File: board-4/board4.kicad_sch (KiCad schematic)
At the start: 101 parts, among them CN1 B2B-PH-K-S(LF)(SN), Q1 DMG3415U, SW1 B3U-1000P, SW2 B3U-1000P, U1 SY8088IAAC, U10 AT42QT1011-TSHR, U12 MX35LF1GE4AB-Z4ITR, U3 MCP73831T-2ACI/OT, U4 TPS61022RWUR, U5 ESP32-S3-MINI-1-N4R2, U6 SN74LV1T34DBVR, U7 MAX98357AETE+T, U8 SPH0655LM4H-1-8, U9 MAX17048G+T10

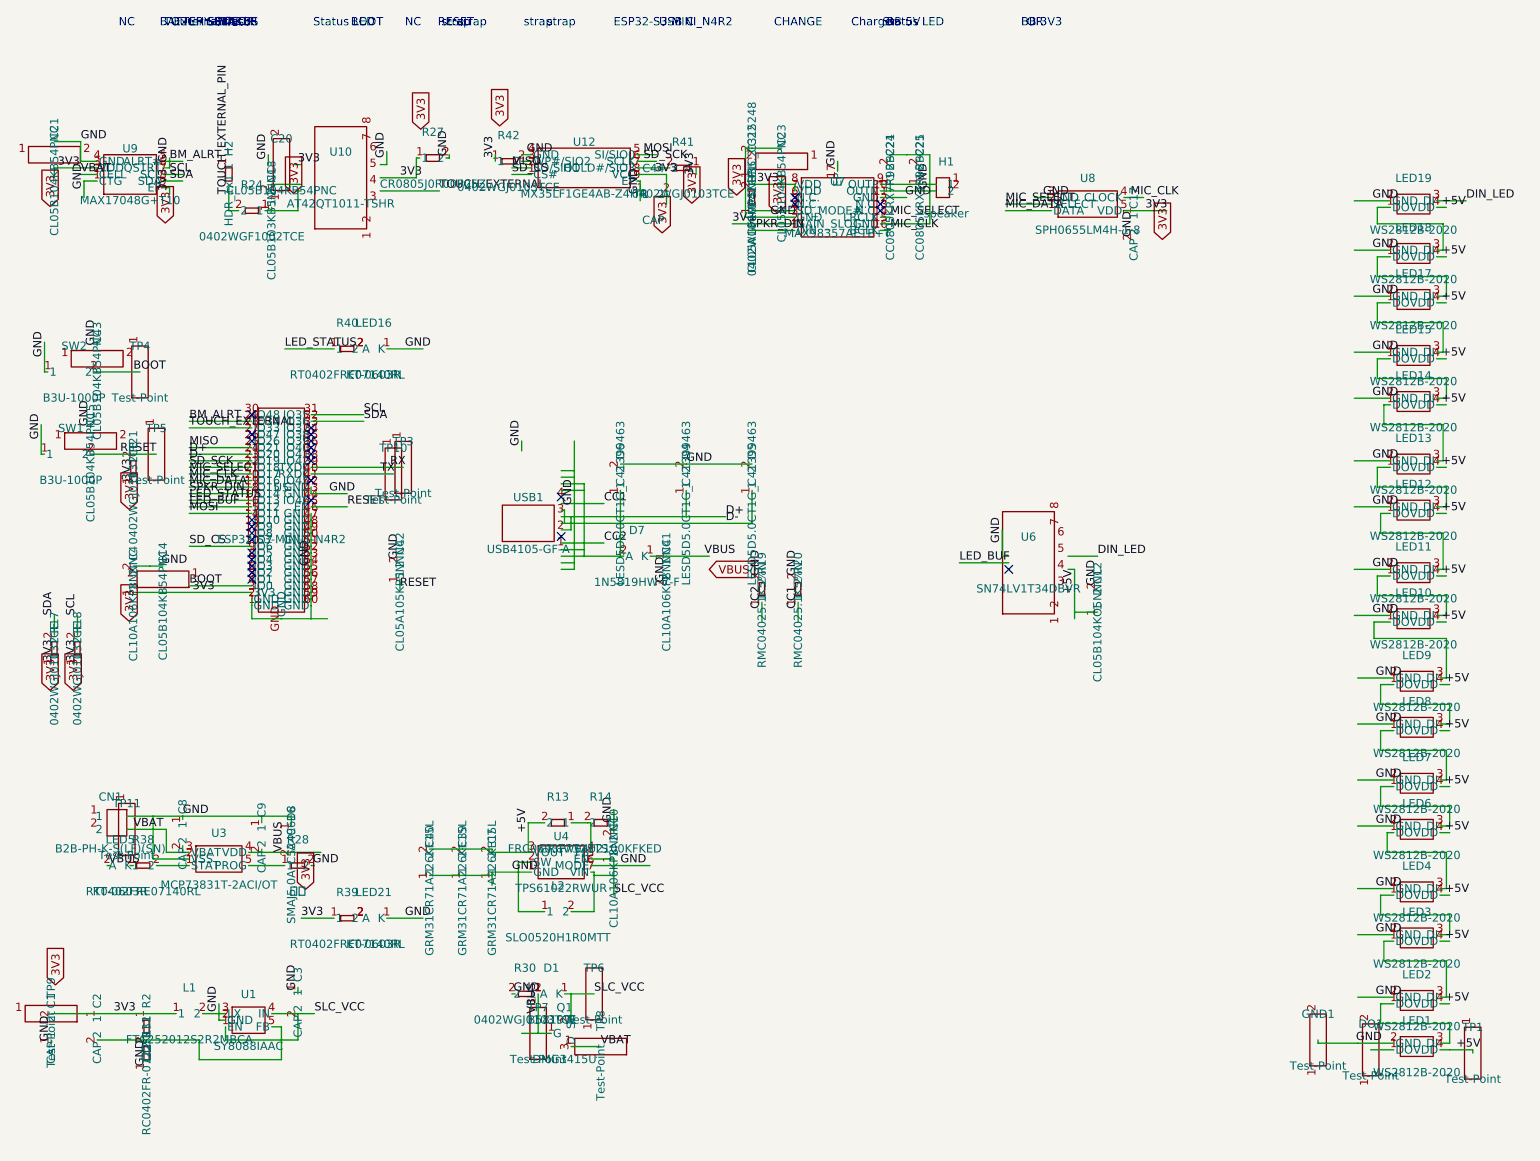
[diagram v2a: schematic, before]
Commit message: Schematic: device-table fallback for symbol UUIDs — 44/44 components now use real .esym geometry (was 39/44, the 5 missing had no explicit Symbol attr). Wire endpoints should now land on real pin offsets.
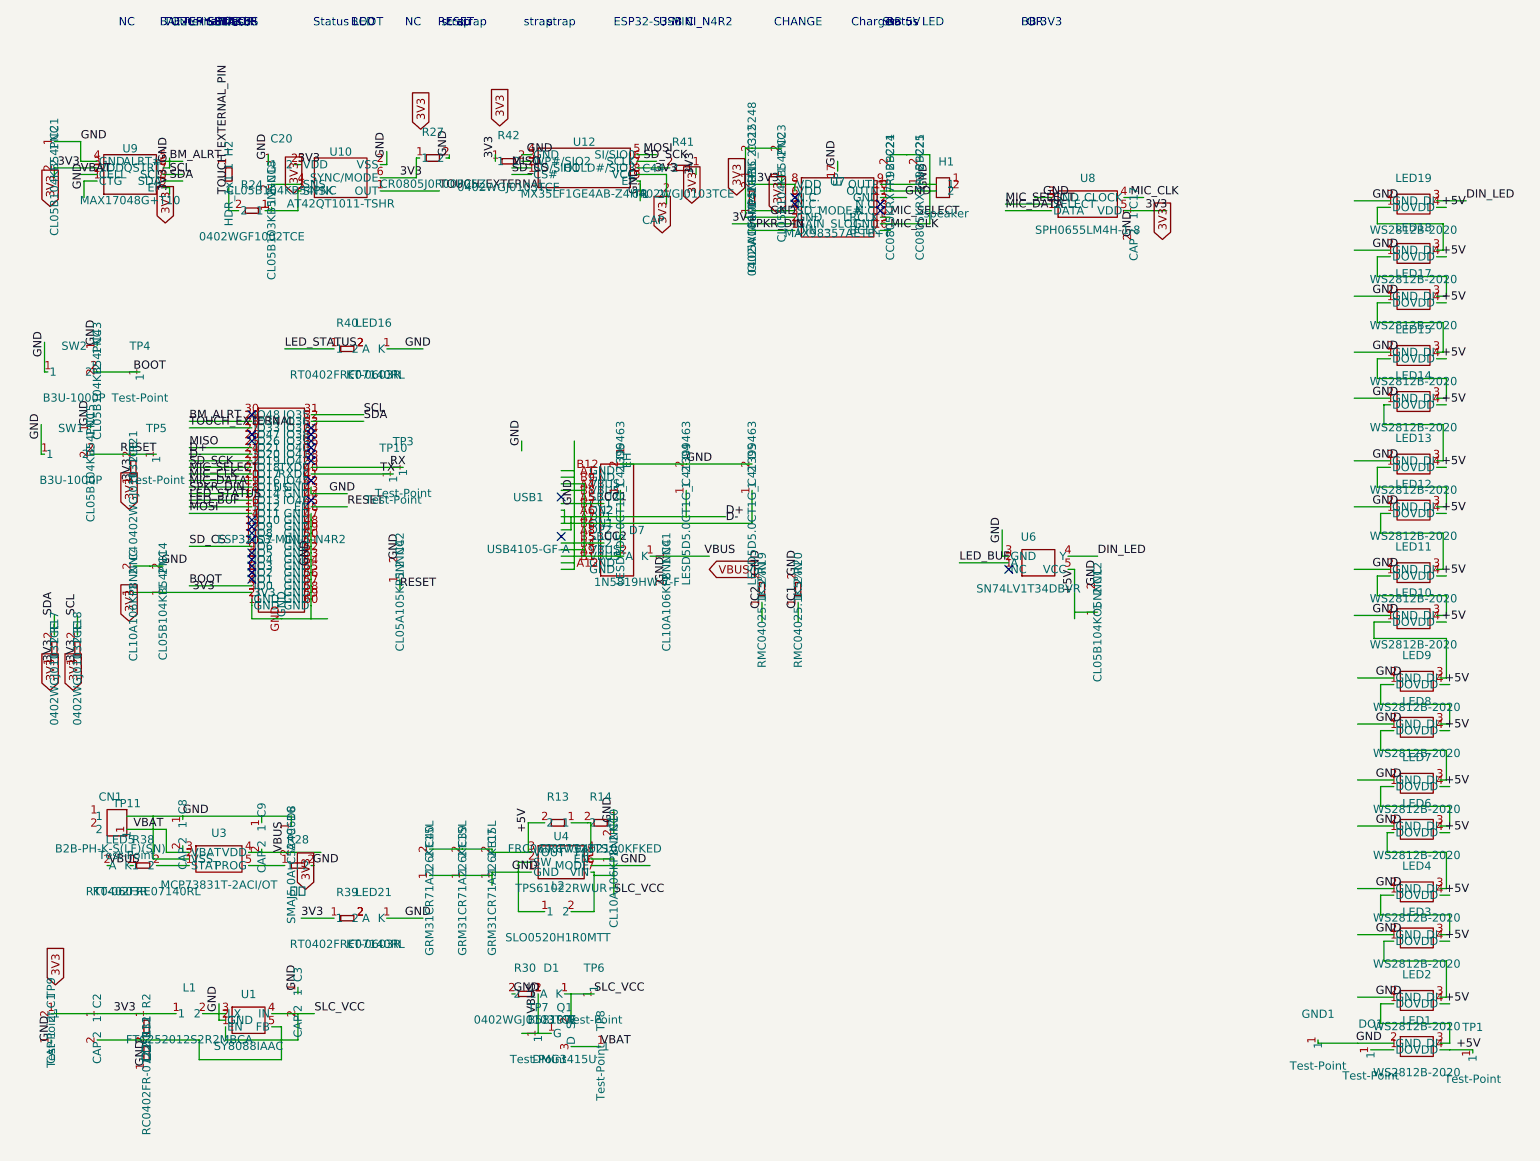
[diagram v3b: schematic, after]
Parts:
- removed C14, C15, C20, C21, C23, C43: CL05B104KB54PNC, symbol Device:C
- removed DO1, GND1: Test-Point, symbol Device:R
- removed TP1, TP10, TP11, TP3, TP4, TP5, TP6, TP7, TP8, TP9: Test-Point, symbol Connector:TestPoint
- removed U10: AT42QT1011-TSHR, symbol Connector_Generic:Conn_01x08
- removed U6: SN74LV1T34DBVR, symbol Connector_Generic:Conn_01x08
- removed USB1: USB4105-GF-A, symbol Connector:Conn_01x04
- added C14, C15, C20, C21, C23, C43: CL05B104KB54PNC, symbol EasyEDA:CL05B104KB54PNC_60ce6391
- added DO1, GND1, TP1, TP10, TP11, TP3, TP4, TP5, TP6, TP7, TP8, TP9: Test-Point, symbol EasyEDA:Test-Point_d3c66d09
- added U10: AT42QT1011-TSHR, symbol EasyEDA:AT42QT1011-TSHR_8e49ab62
- added U6: SN74LV1T34DBVR, symbol EasyEDA:SN74LV1T34DBVR_1921819d
- added USB1: USB4105-GF-A, symbol EasyEDA:USB4105-GF-A_00c7349c
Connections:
- net +5V: now also TP1.1, U6.5 (VCC)
- net 3V3: now also C14.1, C20.2, C21.2, C23.1, TP9.1, U10.5 (VDD), U10.6 (SYNC/MODE)
- net BM_ALRT: now also C14.2, C15.1, C20.1, C21.1, C23.2, C43.1, GND1.1, U10.2 (VSS), U6.3 (GND)
- net BOOT: now also C43.2, TP4.1
- net DIN_LED: now also U6.4 (Y)
- net LED_BUF: now also U6.2 (A)
- net RESET: now also C15.2, TP5.1
- net RX: now also TP3.1
- net SLC_VCC: now also TP6.1
- net TOUCH_EXTERNAL: now also U10.1 (OUT)
- net TX: now also TP10.1
- net VBAT: now also TP11.1, TP8.1
- net VBUS: now also TP7.1
- net at C18.1, R24.1: now also U10.3 (SNSK)
- net at LED1.1 (DO): now also DO1.1
- net at C18.2: now also U10.4 (SNS)
